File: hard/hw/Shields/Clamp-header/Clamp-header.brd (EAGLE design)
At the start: 91.4 x 59.5 mm, 26 parts, among them J1 6p-2.54-90d, J10 6p-SMD-2.54, J11 6p-smd-2.54-90d, J12 6p-2.54-90d, J13 6p-2.54-90d, J14 6p-SMD-2.54, J2 6p-smd-2.54-90d, J3 6p-smd-2.54-90d, J4 6p-SMD-2.54, J5 6p-2.54-90d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

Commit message: Terminado Shield
by Ruben
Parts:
- moved J14 6.67 mm to (83.6, 11.5)
- moved J12 6.67 mm to (83.6, 0.70), flipped to the bottom, turned to 270 degrees
- moved J13 6.67 mm to (68.3, 0.70), flipped to the bottom, turned to 270 degrees
- moved J11 6.67 mm to (68.3, 12.8)
- moved J3 6.51 mm to (68.2, 62.7)
- moved J6 6.51 mm to (68.2, 50.6), flipped to the bottom, turned to 270 degrees
- moved J4 6.51 mm to (83.4, 61.4)
- moved J5 6.51 mm to (83.4, 50.6), flipped to the bottom, turned to 270 degrees
- moved J2 5.02 mm to (28.1, 44.4)
- moved U$1 5.02 mm to (21.7, 60.5)
- moved U$2 5.02 mm to (6.86, 44.0)
- moved U$3 5.02 mm to (49.3, 44.0)
- moved U$5 5.02 mm to (11.4, 53.7)
- moved U$6 5.02 mm to (44.7, 53.7)
- moved U$7 5.02 mm to (34.4, 60.5)
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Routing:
- removed copper zone on layer 16, net GND
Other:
- board size 91.4 x 59.5 mm -> 98.3 x 70.1 mm

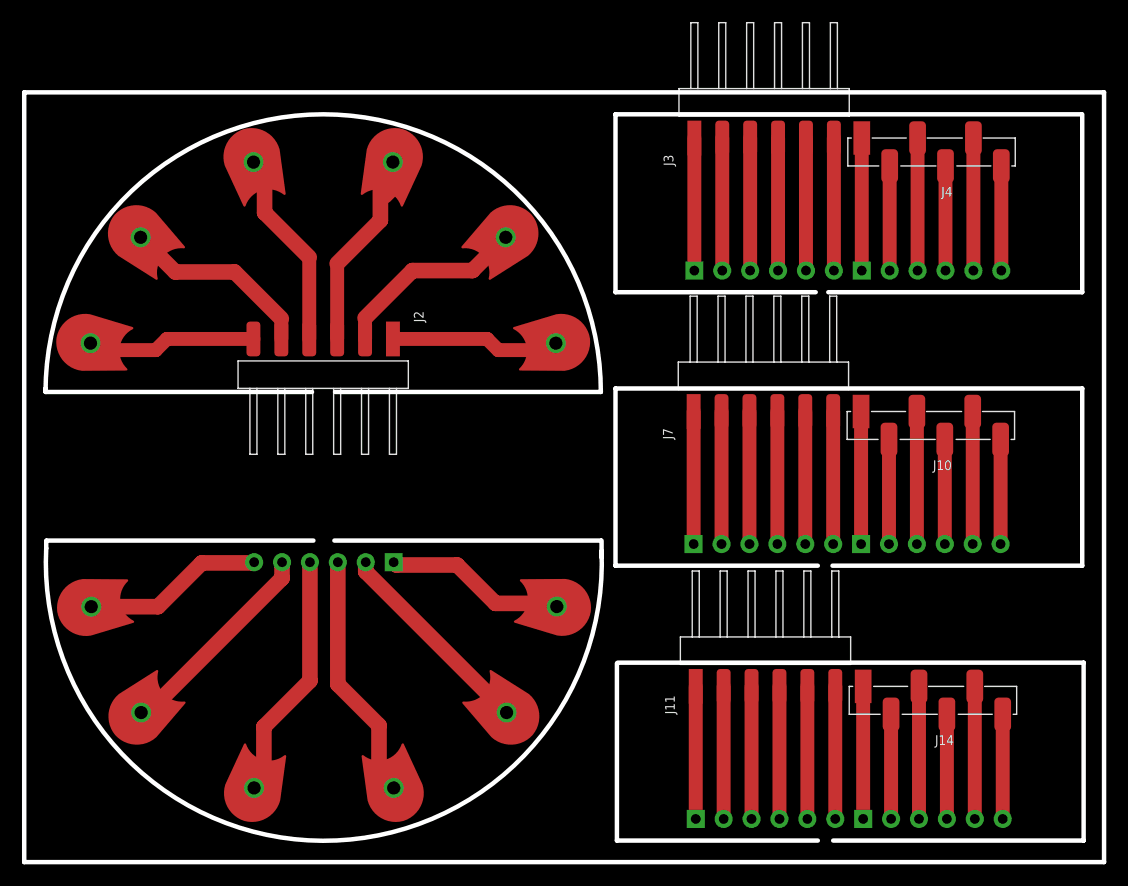
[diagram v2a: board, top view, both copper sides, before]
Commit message: Correccion Shield Clamp
by Ruben
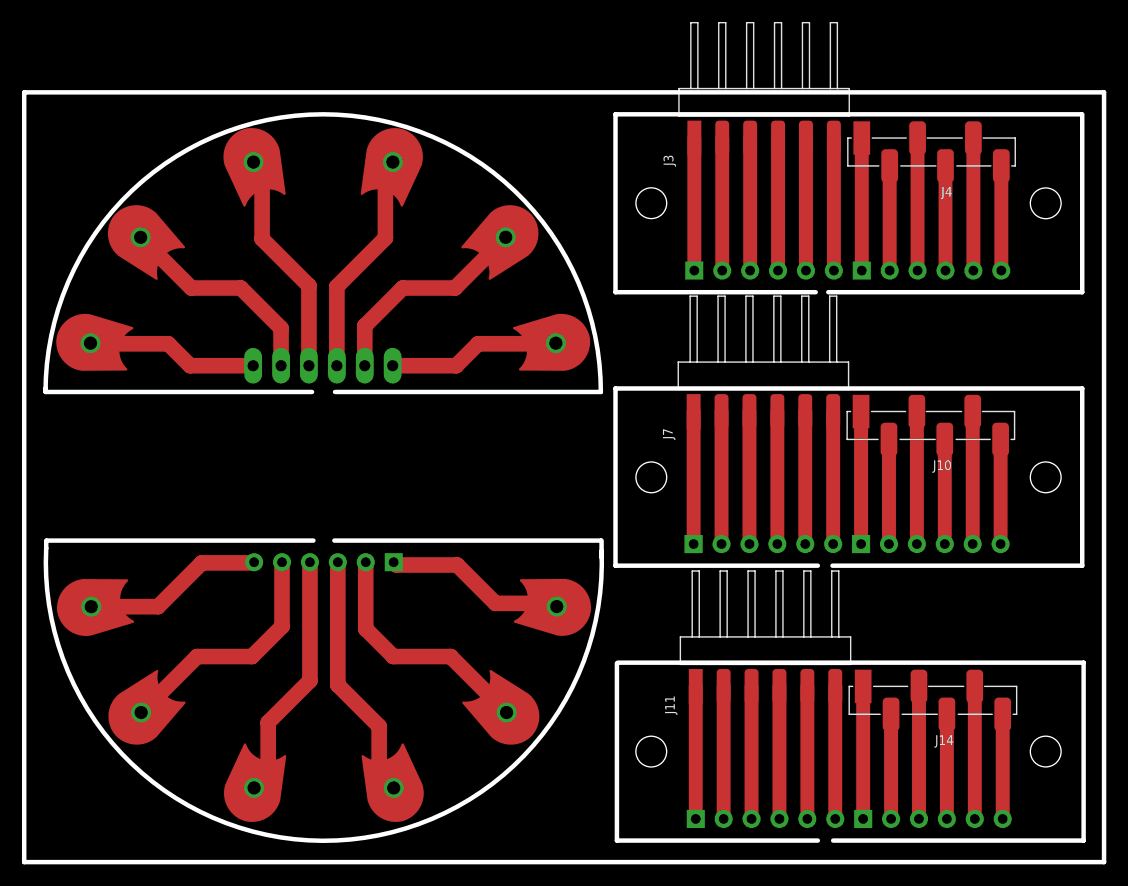
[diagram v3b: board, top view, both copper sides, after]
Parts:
- removed J2: 6p-smd-2.54-90d, Seeed-OPL-Connector:H6-SMD-MALE-2.54-90D
- added JP1: (no value), pinhead:1X06/90
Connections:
- net N$10: now also JP1.3, U$1.1; no longer J2.3, U$7.1
- net N$11: now also JP1.2, U$5.1; no longer J2.2, U$6.1
- net N$12: now also JP1.1, U$2.1; no longer J2.1, U$3.1
- net N$7: now also JP1.6, U$3.1; no longer J2.4, U$1.1
- net N$8: now also JP1.5, U$6.1; no longer J2.6, U$2.1
- net N$9: now also JP1.4, U$7.1; no longer J2.5, U$5.1
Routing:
- net N$8: track 15.5 -> 19.8 mm
- net N$10: track 24.6 -> 20.6 mm
- net N$7: track 19.6 -> 15.7 mm
- net N$5: track 19.0 -> 22.0 mm
- net N$9: track 17.7 -> 20.6 mm
- net N$2: track 19.3 -> 21.9 mm
- net N$11: track 17.8 -> 19.6 mm
- net N$12: track 14.6 -> 15.7 mm
- net N$4: track 22.8 -> 23.3 mm
